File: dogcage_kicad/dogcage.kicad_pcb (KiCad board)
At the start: 2 copper layers, 68.6 x 49.8 mm, 17 parts, among them CON1 5V, M1 XBee, P1 Door, P2 Servo, P3 CONN_01X10, P4 CONN_01X10, P5 CONN_01X14, P7 CONN_01X14, Q1 TIP120, SW1 SW_PUSH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

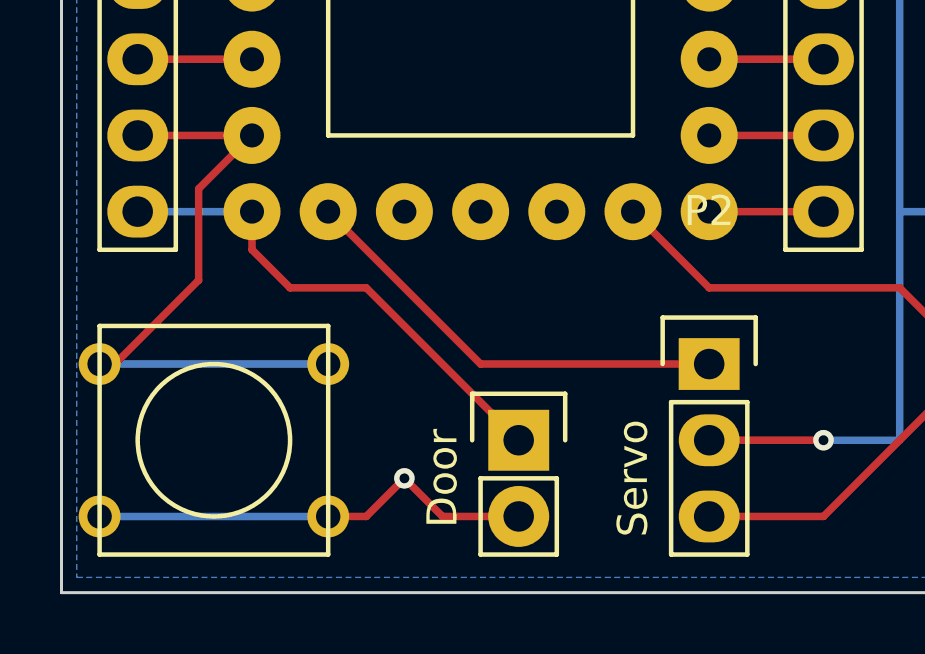
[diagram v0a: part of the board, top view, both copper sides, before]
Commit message: Added 'Trigger' to silkscreen
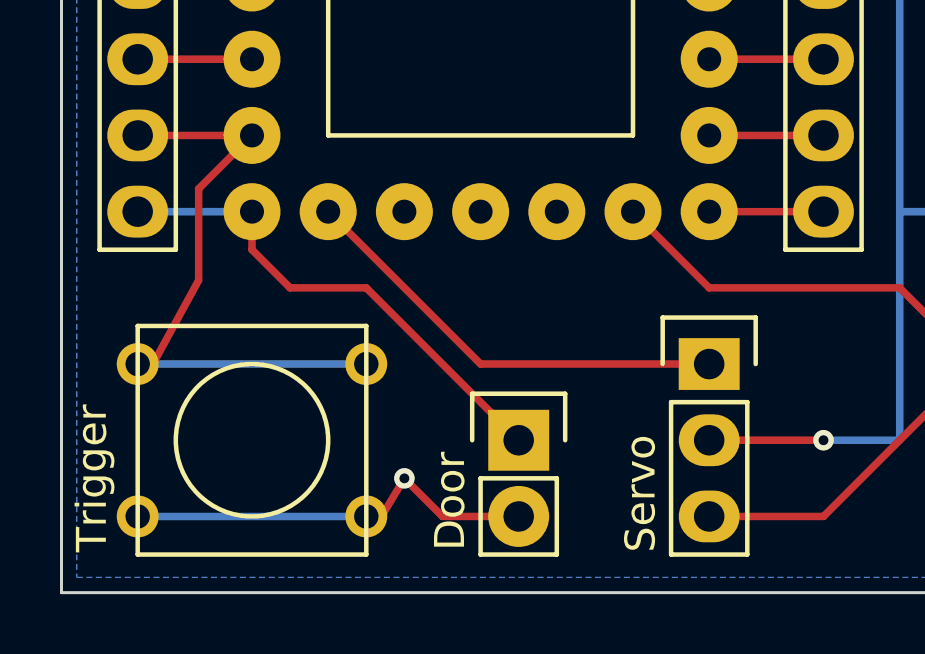
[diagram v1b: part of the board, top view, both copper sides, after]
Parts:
- SW1: value SW_PUSH -> Trigger
- moved SW1 1.27 mm to (135.9, 170.2)
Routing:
- net GND: track 53.7 -> 52.6 mm
- net Net-(P5-Pad13): track 21.5 -> 20.7 mm
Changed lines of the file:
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@@
   )
   (layers
-    (0 F.Cu signal hide)
-    (31 B.Cu signal hide)
-    (36 B.SilkS user hide)
+    (0 F.Cu signal)
+    (31 B.Cu signal)
+    (36 B.SilkS user)
     (37 F.SilkS user)
-    (38 B.Mask user hide)
-    (39 F.Mask user hide)
-    (44 Edge.Cuts user hide)
+    (38 B.Mask user)
+    (39 F.Mask user)
+    (44 Edge.Cuts user)
   )
   (setup
@@
       (effects (font (size 1 1) (thickness 0.15)))
     )
-    (fp_text value Door (at -2.54 1.27 90) (layer F.SilkS)
+    (fp_text value Door (at -2.286 2.032 90) (layer F.SilkS)
       (effects (font (size 1 1) (thickness 0.15)))
     )
@@
     (descr "Through hole pin header")
     (tags "pin header")
-    (fp_text reference P2 (at 0 -5.1) (layer F.SilkS)
-      (effects (font (size 1 1) (thickness 0.15)))
-    )
-    (fp_text value Servo (at -2.54 3.81 90) (layer F.SilkS)
+    (fp_text reference P2 (at 0 -5.1) (layer F.SilkS) hide
+      (effects (font (size 1 1) (thickness 0.15)))
+    )
+    (fp_text value Servo (at -2.286 4.318 90) (layer F.SilkS)
       (effects (font (size 1 1) (thickness 0.15)))
     )
@@
   )
   (module Buttons_Switches_ThroughHole:SW_PUSH_SMALL (layer F.Cu)
-    (at 134.62 170.18)
+    (at 135.89 170.18)
     (fp_text reference SW1 (at 0 -0.762) (layer F.SilkS) hide
       (effects (font (size 1 1) (thickness 0.15)))
     )
-    (fp_text value SW_PUSH (at 0 1.016) (layer F.Fab) hide
+    (fp_text value Trigger (at -5.334 1.27 90) (layer F.SilkS)
       (effects (font (size 1 1) (thickness 0.15)))
     )
@@
   (segment (start 172.72 162.56) (end 172.72 172.72) (width 0.25) (layer B.Cu) (net 1))
   (segment (start 172.72 172.72) (end 168.92524 172.72) (width 0.25) (layer F.Cu) (net 1) (status 20))
+  (segment (start 132.08 172.72) (end 139.7 172.72) (width 0.25) (layer B.Cu) (net 2) (status 30))
   (segment (start 160.528 141.986) (end 160.528 139.7) (width 0.254) (layer F.Cu) (net 2))
   (via (at 159.258 138.43) (size 0.6858) (layers F.Cu B.Cu) (net 2))
@@
   (segment (start 169.34 153.24) (end 166.8 153.24) (width 0.25) (layer F.Cu) (net 2) (status 10))
   (segment (start 142.24 172.72) (end 140.97 171.45) (width 0.25) (layer F.Cu) (net 2))
-  (segment (start 139.7 172.72) (end 138.43 172.72) (width 0.25) (layer F.Cu) (net 2) (status 20))
+  (segment (start 140.208 172.72) (end 139.7 172.72) (width 0.25) (layer F.Cu) (net 2) (status 30))
   (via (at 140.97 171.45) (size 0.6858) (layers F.Cu B.Cu) (net 2))
-  (segment (start 139.7 172.72) (end 140.97 171.45) (width 0.25) (layer F.Cu) (net 2))
+  (segment (start 140.208 172.72) (end 140.97 171.45) (width 0.25) (layer F.Cu) (net 2) (status 10))
   (segment (start 144.78 172.72) (end 142.24 172.72) (width 0.25) (layer F.Cu) (net 2) (status 10))
   (segment (start 168.91 163.08324) (end 168.41724 163.08324) (width 0.25) (layer F.Cu) (net 2) (status 30))
-  (segment (start 130.81 172.72) (end 138.43 172.72) (width 0.25) (layer B.Cu) (net 2) (status 30))
   (segment (start 165.62324 170.70324) (end 165.608 170.688) (width 0.25) (layer F.Cu) (net 2))
   (segment (start 164.846 171.45) (end 161.29 171.45) (width 0.25) (layer F.Cu) (net 2) (status 20))
@@
   (segment (start 135.89 152.4) (end 132.08 152.4) (width 0.25) (layer F.Cu) (net 31) (status 30))
   (segment (start 135.89 154.94) (end 132.08 154.94) (width 0.25) (layer F.Cu) (net 32) (status 30))
+  (segment (start 132.08 167.64) (end 139.7 167.64) (width 0.25) (layer B.Cu) (net 33) (status 30))
   (segment (start 135.89 160.02) (end 132.08 160.02) (width 0.25) (layer F.Cu) (net 33) (status 30))
   (segment (start 134.112 161.798) (end 135.89 160.02) (width 0.25) (layer F.Cu) (net 33) (status 20))
   (segment (start 134.112 164.846) (end 134.112 161.798) (width 0.25) (layer F.Cu) (net 33))
-  (segment (start 131.318 167.64) (end 134.112 164.846) (width 0.25) (layer F.Cu) (net 33) (status 10))
-  (segment (start 130.81 167.64) (end 131.318 167.64) (width 0.25) (layer F.Cu) (net 33) (status 30))
-  (segment (start 130.81 167.64) (end 138.43 167.64) (width 0.25) (layer B.Cu) (net 33) (status 30))
+  (segment (start 132.588 167.64) (end 134.112 164.846) (width 0.25) (layer F.Cu) (net 33) (status 10))
+  (segment (start 132.08 167.64) (end 132.588 167.64) (width 0.25) (layer F.Cu) (net 33) (status 30))
   (segment (start 151.13 132.08) (end 154.94 132.08) (width 0.25) (layer F.Cu) (net 34) (status 30))
   (segment (start 151.13 134.62) (end 154.94 134.62) (width 0.25) (layer F.Cu) (net 35) (status 30))
